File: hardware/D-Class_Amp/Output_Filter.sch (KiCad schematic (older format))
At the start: 5 parts

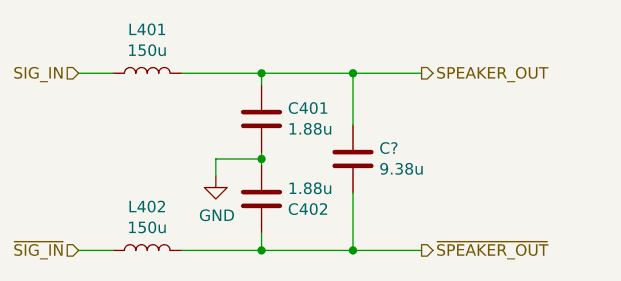
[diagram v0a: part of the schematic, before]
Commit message: Added potentiometer to input gain stage, assigned all input footprints
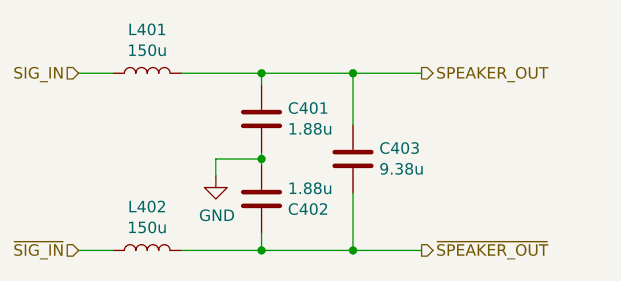
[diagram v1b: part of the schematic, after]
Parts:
- gave numbers to parts that had none: 1
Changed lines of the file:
@@
 	9575 5125 9575 4900
 $Comp
-L Device:C C?
+L Device:C C403
 U 1 1 611BA813
 P 9575 5275
-F 0 "C?" H 9690 5321 50  0000 L CNN
+F 0 "C403" H 9690 5321 50  0000 L CNN
 F 1 "9.38u" H 9690 5230 50  0000 L CNN
 F 2 "" H 9613 5125 50  0001 C CNN

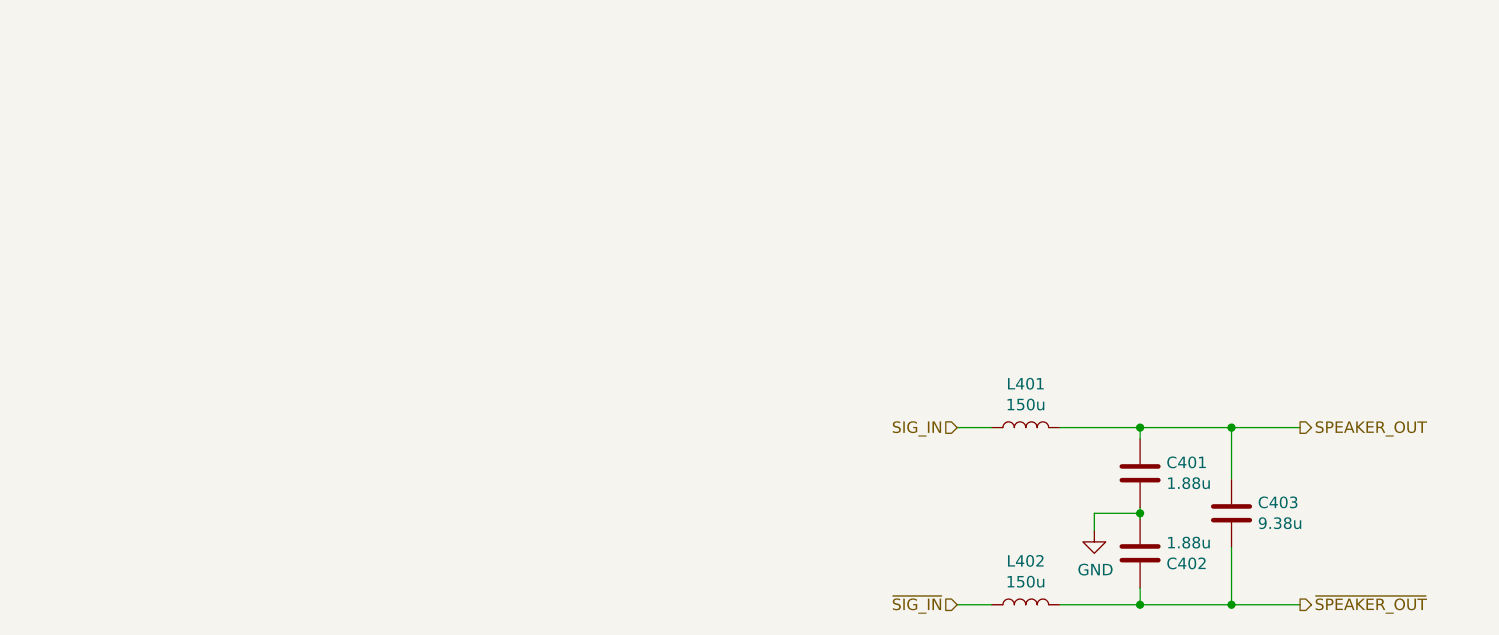
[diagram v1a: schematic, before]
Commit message: Add footprints to the output filter and select output filter components
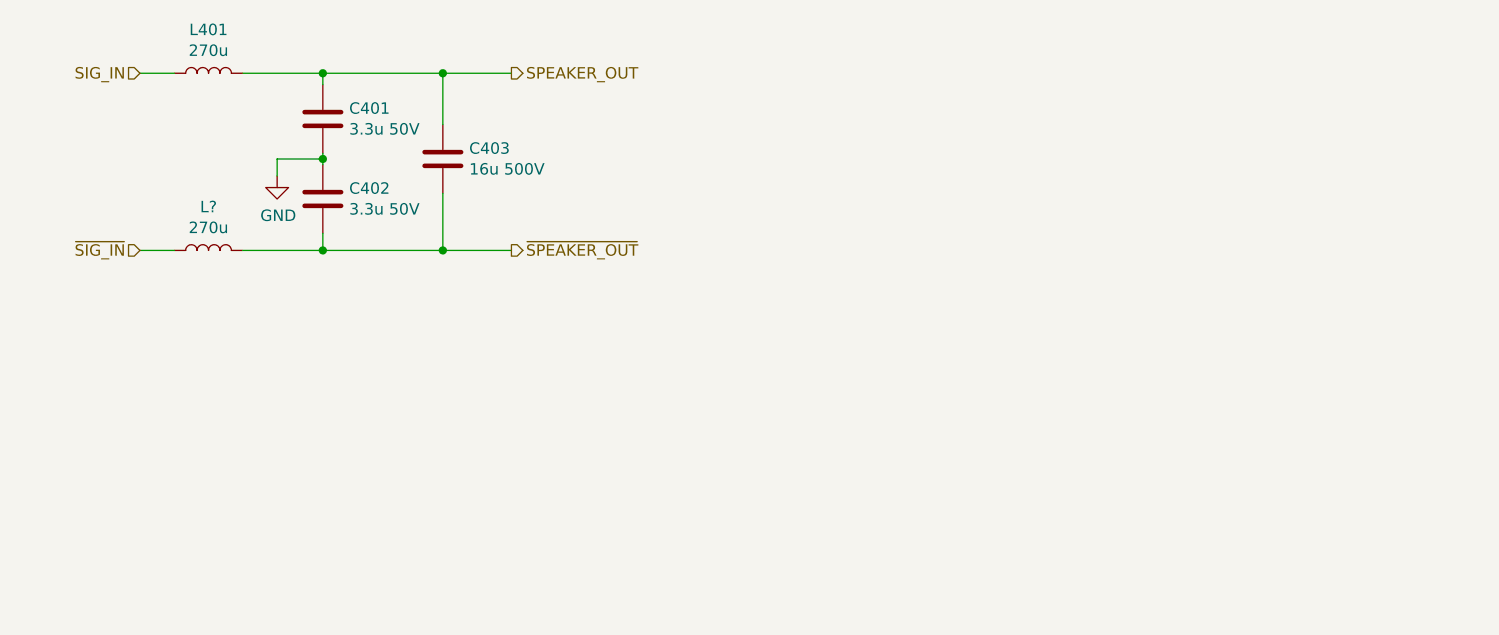
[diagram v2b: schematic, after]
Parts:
- removed L402: 150u, symbol Device:L
- added L?: 270u, Inductor_THT:L_Toroid_Vertical_L31.8mm_W15.9mm_P13.50mm_Bourns_5700, symbol Device:L
- C401, C402: value 1.88u -> 3.3u 50V; footprint (none) -> Capacitor_SMD:CP_Elec_4x5.4; Part Number (none) -> 865080640003
- C403: value 9.38u -> 16u 500V; footprint (none) -> C4AQLLW5160A33K:C4AQLLW5160A33K_film_capacitor; Part Number (none) -> C4AQLLW5160A33K
- L401: value 150u -> 270u; footprint (none) -> Inductor_THT:L_Toroid_Vertical_L31.8mm_W15.9mm_P13.50mm_Bourns_5700; Part Number (none) -> HCTI-270-5.5
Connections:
- net GND: now also C402.1; no longer C402.2
- net ~SIG_IN: now also L?.1
- net ~SPEAKER_OUT: now also C402.2, L?.2; no longer C402.1
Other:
- moved on the sheet: C403, L401
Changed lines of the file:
@@
 Comment4 ""
 $EndDescr
-Text HLabel 8375 4900 0    50   Input ~ 0
+Text HLabel 4800 3350 0    50   Input ~ 0
 SIG_IN
-Text HLabel 8375 5675 0    50   Input ~ 0
+Text HLabel 4800 4125 0    50   Input ~ 0
 ~SIG_IN
 $Comp
 L Device:L L401
 U 1 1 61193FAD
-P 8675 4900
-F 0 "L401" V 8865 4900 50  0000 C CNN
-F 1 "150u" V 8774 4900 50  0000 C CNN
-F 2 "" H 8675 4900 50  0001 C CNN
-F 3 "~" H 8675 4900 50  0001 C CNN
-	1    8675 4900
+P 5100 3350
+F 0 "L401" V 5290 3350 50  0000 C CNN
+F 1 "270u" V 5199 3350 50  0000 C CNN
+F 2 "Inductor_THT:L_Toroid_Vertical_L31.8mm_W15.9mm_P13.50mm_Bourns_5700" H 5100 3350 50  0001 C CNN
+F 3 "https://belfuse.com/resources/datasheets/signaltransformer/ds-st-high-current-torodial-inductors-series.pdf" H 5100 3350 50  0001 C CNN
+F 4 "HCTI-270-5.5" V 5100 3350 50  0001 C CNN "Part Number"
+	1    5100 3350
 	0    -1   -1   0
 $EndComp
+Wire Wire Line
+	4800 3350 4950 3350
+Wire Wire Line
+	5250 3350 5600 3350
+Wire Wire Line
+	5600 3350 5600 3400
+Wire Wire Line
+	5600 3350 6125 3350
+Connection ~ 5600 3350
+Wire Wire Line
+	4800 4125 4950 4125
+Wire Wire Line
+	5250 4125 5600 4125
+Wire Wire Line
+	5600 4125 5600 4050
+Wire Wire Line
+	5600 4125 6125 4125
+Connection ~ 5600 4125
 $Comp
-L Device:L L402
-U 1 1 61195264
-P 8675 5675
-F 0 "L402" V 8865 5675 50  0000 C CNN
-F 1 "150u" V 8774 5675 50  0000 C CNN
-F 2 "" H 8675 5675 50  0001 C CNN
-F 3 "~" H 8675 5675 50  0001 C CNN
-	1    8675 5675
-	0    1    -1   0
+L power:GND #PWR0401
+U 1 1 611D879A
+P 5400 3800
+F 0 "#PWR0401" H 5400 3550 50  0001 C CNN
+F 1 "GND" H 5405 3627 50  0000 C CNN
+F 2 "" H 5400 3800 50  0001 C CNN
+F 3 "" H 5400 3800 50  0001 C CNN
+	1    5400 3800
+	1    0    0    -1
 $EndComp
+Wire Wire Line
+	5600 3750 5600 3725
+Text HLabel 6425 3350 2    50   Output ~ 0
+SPEAKER_OUT
+Text HLabel 6425 4125 2    50   Output ~ 0
+~SPEAKER_OUT
+Wire Wire Line
+	5600 3725 5400 3725
+Wire Wire Line
+	5400 3725 5400 3800
+Connection ~ 5600 3725
+Wire Wire Line
+	5600 3725 5600 3700
+Connection ~ 6125 4125
+Wire Wire Line
+	6125 4125 6425 4125
+Connection ~ 6125 3350
+Wire Wire Line
+	6125 3350 6425 3350
+Wire Wire Line
+	6125 3875 6125 4125
+Wire Wire Line
+	6125 3575 6125 3350
 $Comp
-L Device:C C401
-U 1 1 611955B4
-P 9175 5100
-F 0 "C401" H 9290 5146 50  0000 L CNN
-F 1 "1.88u" H 9290 5055 50  0000 L CNN
-F 2 "" H 9213 4950 50  0001 C CNN
-F 3 "~" H 9175 5100 50  0001 C CNN
-	1    9175 5100
+L Device:C C403
+U 1 1 611BA813
+P 6125 3725
+F 0 "C403" H 6240 3771 50  0000 L CNN
+F 1 "16u 500V" H 6240 3680 50  0000 L CNN
+F 2 "C4AQLLW5160A33K:C4AQLLW5160A33K_film_capacitor" H 6163 3575 50  0001 C CNN
+F 3 "https://content.kemet.com/datasheets/KEM_F3114_C4AQ.pdf" H 6125 3725 50  0001 C CNN
+F 4 "C4AQLLW5160A33K" H 6125 3725 50  0001 C CNN "Part Number"
+	1    6125 3725
 	1    0    0    -1
 $EndComp
 $Comp
 L Device:C C402
-U 1 1 61195DF7
-P 9175 5450
-F 0 "C402" H 9290 5496 50  0000 L CNN
-F 1 "1.88u" H 9290 5405 50  0000 L CNN
-F 2 "" H 9213 5300 50  0001 C CNN
-F 3 "~" H 9175 5450 50  0001 C CNN
-	1    9175 5450
-	1    0    0    1
-$EndComp
-Wire Wire Line
-	8375 4900 8525 4900
-Wire Wire Line
-	8825 4900 9175 4900
-Wire Wire Line
-	9175 4900 9175 4950
-Wire Wire Line
-	9175 4900 9575 4900
-Connection ~ 9175 4900
-Wire Wire Line
-	8375 5675 8525 5675
-Wire Wire Line
-	8825 5675 9175 5675
-Wire Wire Line
-	9175 5675 9175 5600
-Wire Wire Line
-	9175 5675 9575 5675
-Connection ~ 9175 5675
-$Comp
-L power:GND #PWR0401
-U 1 1 611D879A
-P 8975 5350
-F 0 "#PWR0401" H 8975 5100 50  0001 C CNN
-F 1 "GND" H 8980 5177 50  0000 C CNN
-F 2 "" H 8975 5350 50  0001 C CNN
-F 3 "" H 8975 5350 50  0001 C CNN
-	1    8975 5350
+U 1 1 611597AC
+P 5600 3900
+F 0 "C402" H 5715 3946 50  0000 L CNN
+F 1 "3.3u 50V" H 5715 3855 50  0000 L CNN
+F 2 "Capacitor_SMD:CP_Elec_4x5.4" H 5638 3750 50  0001 C CNN
+F 3 "https://www.we-online.de/katalog/datasheet/865080640003.pdf" H 5600 3900 50  0001 C CNN
+F 4 "865080640003" H 5600 3900 50  0001 C CNN "Part Number"
+	1    5600 3900
 	1    0    0    -1
 $EndComp
-Wire Wire Line
-	9175 5300 9175 5275
-Text HLabel 9875 4900 2    50   Output ~ 0
-SPEAKER_OUT
-Text HLabel 9875 5675 2    50   Output ~ 0
-~SPEAKER_OUT
-Wire Wire Line
-	9175 5275 8975 5275
-Wire Wire Line
-	8975 5275 8975 5350
-Connection ~ 9175 5275
-Wire Wire Line
-	9175 5275 9175 5250
-Connection ~ 9575 5675
-Wire Wire Line
-	9575 5675 9875 5675
-Connection ~ 9575 4900
-Wire Wire Line
-	9575 4900 9875 4900
-Wire Wire Line
-	9575 5425 9575 5675
-Wire Wire Line
-	9575 5125 9575 4900
 $Comp
-L Device:C C403
-U 1 1 611BA813
-P 9575 5275
-F 0 "C403" H 9690 5321 50  0000 L CNN
-F 1 "9.38u" H 9690 5230 50  0000 L CNN
-F 2 "" H 9613 5125 50  0001 C CNN
-F 3 "~" H 9575 5275 50  0001 C CNN
-	1    9575 5275
+L Device:C C401
+U 1 1 61159C4A
+P 5600 3550
+F 0 "C401" H 5715 3596 50  0000 L CNN
+F 1 "3.3u 50V" H 5715 3505 50  0000 L CNN
+F 2 "Capacitor_SMD:CP_Elec_4x5.4" H 5638 3400 50  0001 C CNN
+F 3 "https://www.we-online.de/katalog/datasheet/865080640003.pdf" H 5600 3550 50  0001 C CNN
+F 4 "865080640003" H 5600 3550 50  0001 C CNN "Part Number"
+	1    5600 3550
 	1    0    0    -1
 $EndComp
+$Comp
+L Device:L L?
+U 1 1 6115F7AF
+P 5100 4125
+F 0 "L?" V 5290 4125 50  0000 C CNN
+F 1 "270u" V 5199 4125 50  0000 C CNN
+F 2 "Inductor_THT:L_Toroid_Vertical_L31.8mm_W15.9mm_P13.50mm_Bourns_5700" H 5100 4125 50  0001 C CNN
+F 3 "https://belfuse.com/resources/datasheets/signaltransformer/ds-st-high-current-torodial-inductors-series.pdf" H 5100 4125 50  0001 C CNN
+F 4 "HCTI-270-5.5" V 5100 4125 50  0001 C CNN "Part Number"
+	1    5100 4125
+	0    -1   -1   0
+$EndComp
 $EndSCHEMATC

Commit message: Updated and fixed the input filter schematic
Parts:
- gave numbers to parts that had none: 1
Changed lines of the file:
@@
 $EndComp
 $Comp
-L Device:L L?
+L Device:L L1
 U 1 1 6115F7AF
 P 5100 4125
-F 0 "L?" V 5290 4125 50  0000 C CNN
+F 0 "L1" V 5290 4125 50  0000 C CNN
 F 1 "270u" V 5199 4125 50  0000 C CNN
 F 2 "Inductor_THT:L_Toroid_Vertical_L31.8mm_W15.9mm_P13.50mm_Bourns_5700" H 5100 4125 50  0001 C CNN

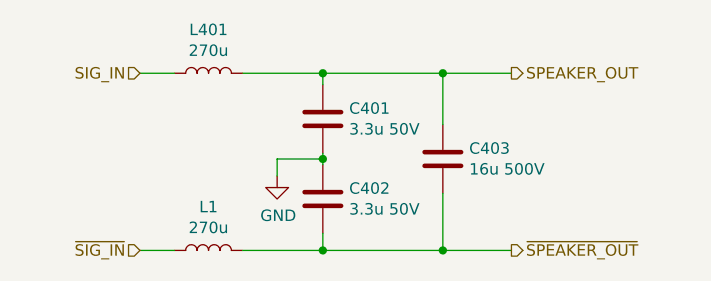
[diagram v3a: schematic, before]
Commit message: added pricing and and part numbers to all components
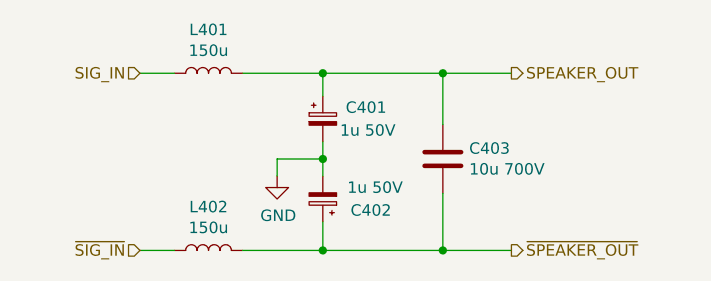
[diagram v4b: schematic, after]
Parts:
- removed C401, C402: 3.3u 50V, Capacitor_SMD:CP_Elec_4x5.4, symbol Device:C
- removed L1: 270u, Inductor_THT:L_Toroid_Vertical_L31.8mm_W15.9mm_P13.50mm_Bourns_5700, symbol Device:L
- added C401, C402: 1u 50V, Capacitor_SMD:CP_Elec_4x5.4, symbol Device:CP_Small
- added L402: 150u, IND_HCTI-150-5.0:IND_HCTI-150-5.0, symbol Device:L
- C403: value 16u 500V -> 10u 700V; footprint C4AQLLW5160A33K:C4AQLLW5160A33K_film_capacitor -> C4AQJLU5100M19J:C4AQJLU5100M19J_film_capacitor; DigiKey Price (none) -> 5.67; Part Number C4AQLLW5160A33K -> C4AQJLU5100M19J
- L401: value 270u -> 150u; footprint Inductor_THT:L_Toroid_Vertical_L31.8mm_W15.9mm_P13.50mm_Bourns_5700 -> IND_HCTI-150-5.0:IND_HCTI-150-5.0; DigiKey Price (none) -> 4.20; Part Number HCTI-270-5.5 -> HCTI-150-5.0
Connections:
- net GND: now also C401.2, C402.2
- net SPEAKER_OUT: now also C401.1
- net ~SIG_IN: now also L402.1
- net ~SPEAKER_OUT: now also C402.1, L402.2
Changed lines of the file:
@@
 P 5100 3350
 F 0 "L401" V 5290 3350 50  0000 C CNN
-F 1 "270u" V 5199 3350 50  0000 C CNN
-F 2 "Inductor_THT:L_Toroid_Vertical_L31.8mm_W15.9mm_P13.50mm_Bourns_5700" H 5100 3350 50  0001 C CNN
+F 1 "150u" V 5199 3350 50  0000 C CNN
+F 2 "IND_HCTI-150-5.0:IND_HCTI-150-5.0" H 5100 3350 50  0001 C CNN
 F 3 "https://belfuse.com/resources/datasheets/signaltransformer/ds-st-high-current-torodial-inductors-series.pdf" H 5100 3350 50  0001 C CNN
-F 4 "HCTI-270-5.5" V 5100 3350 50  0001 C CNN "Part Number"
+F 4 "HCTI-150-5.0" V 5100 3350 50  0001 C CNN "Part Number"
+F 5 "4.20" H 5100 3350 50  0001 C CNN "DigiKey Price"
 	1    5100 3350
 	0    -1   -1   0
@@
 	5250 3350 5600 3350
 Wire Wire Line
-	5600 3350 5600 3400
-Wire Wire Line
 	5600 3350 6125 3350
 Connection ~ 5600 3350
@@
 Wire Wire Line
 	5250 4125 5600 4125
-Wire Wire Line
-	5600 4125 5600 4050
 Wire Wire Line
 	5600 4125 6125 4125
@@
 	1    0    0    -1
 $EndComp
-Wire Wire Line
-	5600 3750 5600 3725
 Text HLabel 6425 3350 2    50   Output ~ 0
 SPEAKER_OUT
@@
 	5400 3725 5400 3800
 Connection ~ 5600 3725
-Wire Wire Line
-	5600 3725 5600 3700
 Connection ~ 6125 4125
 Wire Wire Line
@@
 P 6125 3725
 F 0 "C403" H 6240 3771 50  0000 L CNN
-F 1 "16u 500V" H 6240 3680 50  0000 L CNN
-F 2 "C4AQLLW5160A33K:C4AQLLW5160A33K_film_capacitor" H 6163 3575 50  0001 C CNN
-F 3 "https://content.kemet.com/datasheets/KEM_F3114_C4AQ.pdf" H 6125 3725 50  0001 C CNN
-F 4 "C4AQLLW5160A33K" H 6125 3725 50  0001 C CNN "Part Number"
+F 1 "10u 700V" H 6240 3680 50  0000 L CNN
+F 2 "C4AQJLU5100M19J:C4AQJLU5100M19J_film_capacitor" H 6163 3575 50  0001 C CNN
+F 3 "https://content.kemet.com/datasheets/KEM_F3125_C4AQ_M.pdf" H 6125 3725 50  0001 C CNN
+F 4 "C4AQJLU5100M19J" H 6125 3725 50  0001 C CNN "Part Number"
+F 5 "5.67" H 6125 3725 50  0001 C CNN "DigiKey Price"
 	1    6125 3725
 	1    0    0    -1
 $EndComp
 $Comp
-L Device:C C402
-U 1 1 611597AC
+L Device:CP_Small C402
+U 1 1 611418FA
 P 5600 3900
-F 0 "C402" H 5715 3946 50  0000 L CNN
-F 1 "3.3u 50V" H 5715 3855 50  0000 L CNN
+F 0 "C402" H 5300 3950 50  0000 L CNN
+F 1 "1u 50V" H 5250 3850 50  0000 L CNN
 F 2 "Capacitor_SMD:CP_Elec_4x5.4" H 5638 3750 50  0001 C CNN
-F 3 "https://www.we-online.de/katalog/datasheet/865080640003.pdf" H 5600 3900 50  0001 C CNN
-F 4 "865080640003" H 5600 3900 50  0001 C CNN "Part Number"
+F 3 "https://www.we-online.de/katalog/datasheet/865080640001.pdf" H 5600 3900 50  0001 C CNN
+F 4 "865080640001" H 5600 3900 50  0001 C CNN "Part Number"
+F 5 "0.29" H 5600 3900 50  0001 C CNN "DigiKey Price"
 	1    5600 3900
-	1    0    0    -1
+	-1   0    0    1
 $EndComp
 $Comp
-L Device:C C401
-U 1 1 61159C4A
+L Device:L L402
+U 1 1 61143B07
+P 5100 4125
+F 0 "L402" V 5290 4125 50  0000 C CNN
+F 1 "150u" V 5199 4125 50  0000 C CNN
+F 2 "IND_HCTI-150-5.0:IND_HCTI-150-5.0" H 5100 4125 50  0001 C CNN
+F 3 "https://belfuse.com/resources/datasheets/signaltransformer/ds-st-high-current-torodial-inductors-series.pdf" H 5100 4125 50  0001 C CNN
+F 4 "HCTI-150-5.0" V 5100 4125 50  0001 C CNN "Part Number"
+F 5 "4.20" H 5100 4125 50  0001 C CNN "DigiKey Price"
+	1    5100 4125
+	0    -1   -1   0
+$EndComp
+Wire Wire Line
+	5600 4000 5600 4125
+Wire Wire Line
+	5600 3725 5600 3800
+$Comp
+L Device:CP_Small C401
+U 1 1 613470A8
 P 5600 3550
-F 0 "C401" H 5715 3596 50  0000 L CNN
-F 1 "3.3u 50V" H 5715 3505 50  0000 L CNN
+F 0 "C401" H 5700 3600 50  0000 L CNN
+F 1 "1u 50V" H 5675 3500 50  0000 L CNN
 F 2 "Capacitor_SMD:CP_Elec_4x5.4" H 5638 3400 50  0001 C CNN
-F 3 "https://www.we-online.de/katalog/datasheet/865080640003.pdf" H 5600 3550 50  0001 C CNN
-F 4 "865080640003" H 5600 3550 50  0001 C CNN "Part Number"
+F 3 "https://www.we-online.de/katalog/datasheet/865080640001.pdf" H 5600 3550 50  0001 C CNN
+F 4 "865080640001" H 5600 3550 50  0001 C CNN "Part Number"
+F 5 "0.29" H 5600 3550 50  0001 C CNN "DigiKey Price"
 	1    5600 3550
 	1    0    0    -1
 $EndComp
-$Comp
-L Device:L L1
-U 1 1 6115F7AF
-P 5100 4125
-F 0 "L1" V 5290 4125 50  0000 C CNN
-F 1 "270u" V 5199 4125 50  0000 C CNN
-F 2 "Inductor_THT:L_Toroid_Vertical_L31.8mm_W15.9mm_P13.50mm_Bourns_5700" H 5100 4125 50  0001 C CNN
-F 3 "https://belfuse.com/resources/datasheets/signaltransformer/ds-st-high-current-torodial-inductors-series.pdf" H 5100 4125 50  0001 C CNN
-F 4 "HCTI-270-5.5" V 5100 4125 50  0001 C CNN "Part Number"
-	1    5100 4125
-	0    -1   -1   0
-$EndComp
+Wire Wire Line
+	5600 3350 5600 3450
+Wire Wire Line
+	5600 3650 5600 3725
 $EndSCHEMATC

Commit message: readded art and regen bom
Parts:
- C401, C402: symbol Device:CP_Small -> D-Class_Amp-rescue:CP_Small-Device
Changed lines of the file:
@@
 $EndComp
 $Comp
-L Device:CP_Small C402
+L D-Class_Amp-rescue:CP_Small-Device C402
 U 1 1 611418FA
 P 5600 3900
@@
 	5600 3725 5600 3800
 $Comp
-L Device:CP_Small C401
+L D-Class_Amp-rescue:CP_Small-Device C401
 U 1 1 613470A8
 P 5600 3550
